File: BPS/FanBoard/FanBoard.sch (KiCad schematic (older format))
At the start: 12 parts, among them J1 Conn_01x02, J2 Conn_01x02, J3 Conn_01x02, J4 Conn_01x02, Q1 BUK9M34-100EX, Q2 BUK9M34-100EX, Q3 BUK9M34-100EX, Q4 BUK9M34-100EX

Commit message: Finished PCB
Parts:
- J1, J2, J3, J4: footprint (none) -> Connector_PinSocket_2.54mm:PinSocket_1x02_P2.54mm_Vertical
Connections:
- net at J1.2 (Pin_2), Q1.5 (D): now also D1.2 (A)
- net at J3.2 (Pin_2), Q3.5 (D): now also D3.2 (A)
- net at J4.2 (Pin_2), Q4.5 (D): now also D4.2 (A)
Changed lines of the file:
@@
 F 0 "J1" H 4330 3642 50  0000 L CNN
 F 1 "Conn_01x02" H 4330 3551 50  0000 L CNN
-F 2 "" H 4250 3650 50  0001 C CNN
+F 2 "Connector_PinSocket_2.54mm:PinSocket_1x02_P2.54mm_Vertical" H 4250 3650 50  0001 C CNN
 F 3 "~" H 4250 3650 50  0001 C CNN
 	1    4250 3650
@@
 F 0 "J2" H 4330 4292 50  0000 L CNN
 F 1 "Conn_01x02" H 4330 4201 50  0000 L CNN
-F 2 "" H 4250 4300 50  0001 C CNN
+F 2 "Connector_PinSocket_2.54mm:PinSocket_1x02_P2.54mm_Vertical" H 4250 4300 50  0001 C CNN
 F 3 "~" H 4250 4300 50  0001 C CNN
 	1    4250 4300
@@
 F 0 "J3" H 4330 4942 50  0000 L CNN
 F 1 "Conn_01x02" H 4330 4851 50  0000 L CNN
-F 2 "" H 4250 4950 50  0001 C CNN
+F 2 "Connector_PinSocket_2.54mm:PinSocket_1x02_P2.54mm_Vertical" H 4250 4950 50  0001 C CNN
 F 3 "~" H 4250 4950 50  0001 C CNN
 	1    4250 4950
@@
 F 0 "J4" H 4330 5592 50  0000 L CNN
 F 1 "Conn_01x02" H 4330 5501 50  0000 L CNN
-F 2 "" H 4250 5600 50  0001 C CNN
+F 2 "Connector_PinSocket_2.54mm:PinSocket_1x02_P2.54mm_Vertical" H 4250 5600 50  0001 C CNN
 F 3 "~" H 4250 5600 50  0001 C CNN
 	1    4250 5600
@@
 	3200 4400 3700 4400
 Wire Wire Line
-	3200 5050 4050 5050
-Wire Wire Line
-	3200 3750 4050 3750
+	3200 5050 3700 5050
+Wire Wire Line
+	3200 3750 3700 3750
 NoConn ~ 2900 5900
 NoConn ~ 2900 5250
@@
 $EndComp
 Wire Wire Line
-	3200 5700 4050 5700
+	3200 5700 3750 5700
 Connection ~ 3700 4400
 Wire Wire Line
@@
 Wire Wire Line
 	3950 5400 3950 4950
+Connection ~ 3700 3750
+Wire Wire Line
+	3700 3750 4050 3750
+Connection ~ 3700 5050
+Wire Wire Line
+	3700 5050 4050 5050
+Connection ~ 3750 5700
+Wire Wire Line
+	3750 5700 4050 5700
 $EndSCHEMATC

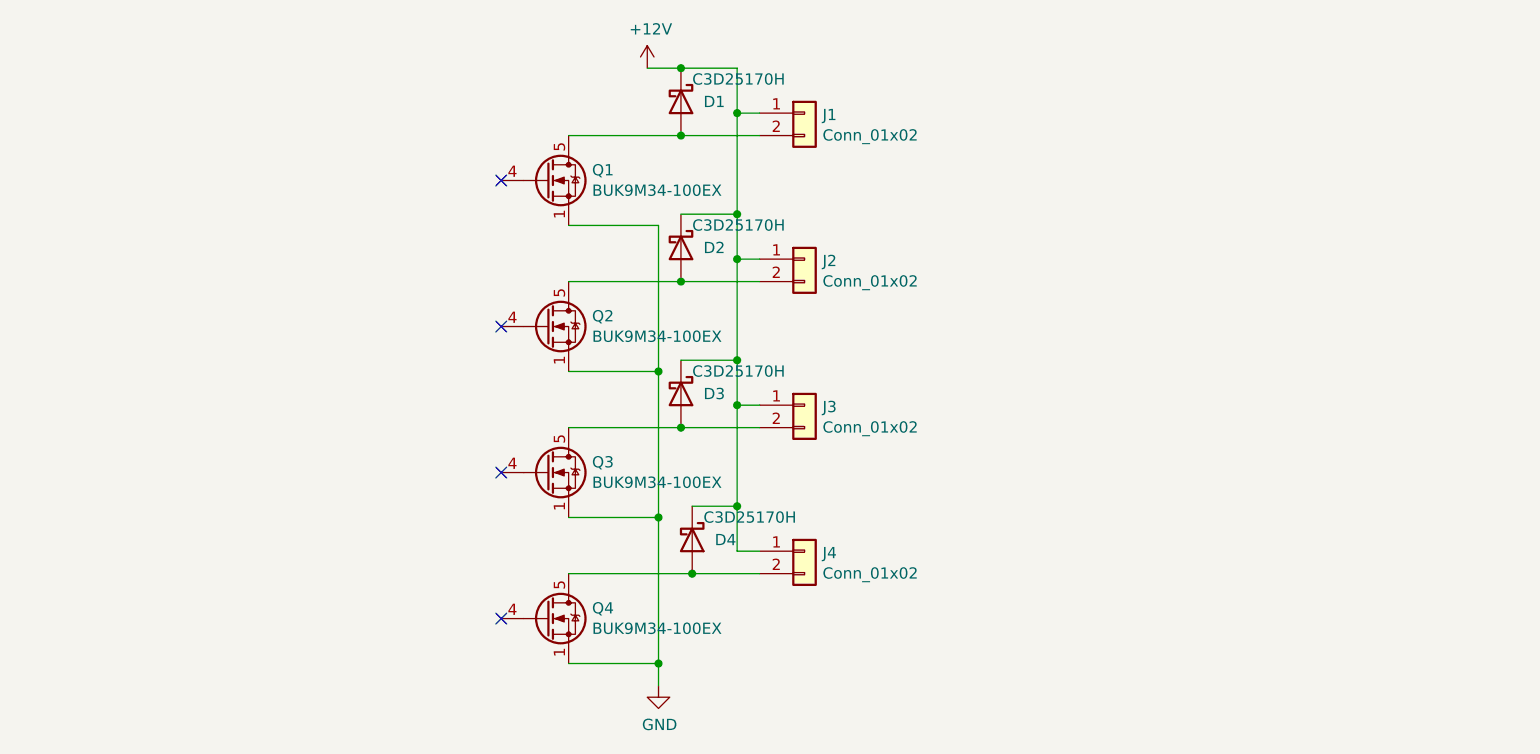
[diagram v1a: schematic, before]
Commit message: Added connections for control, pwr, and ground. Need to add DC-DC converter for 12V to 5V
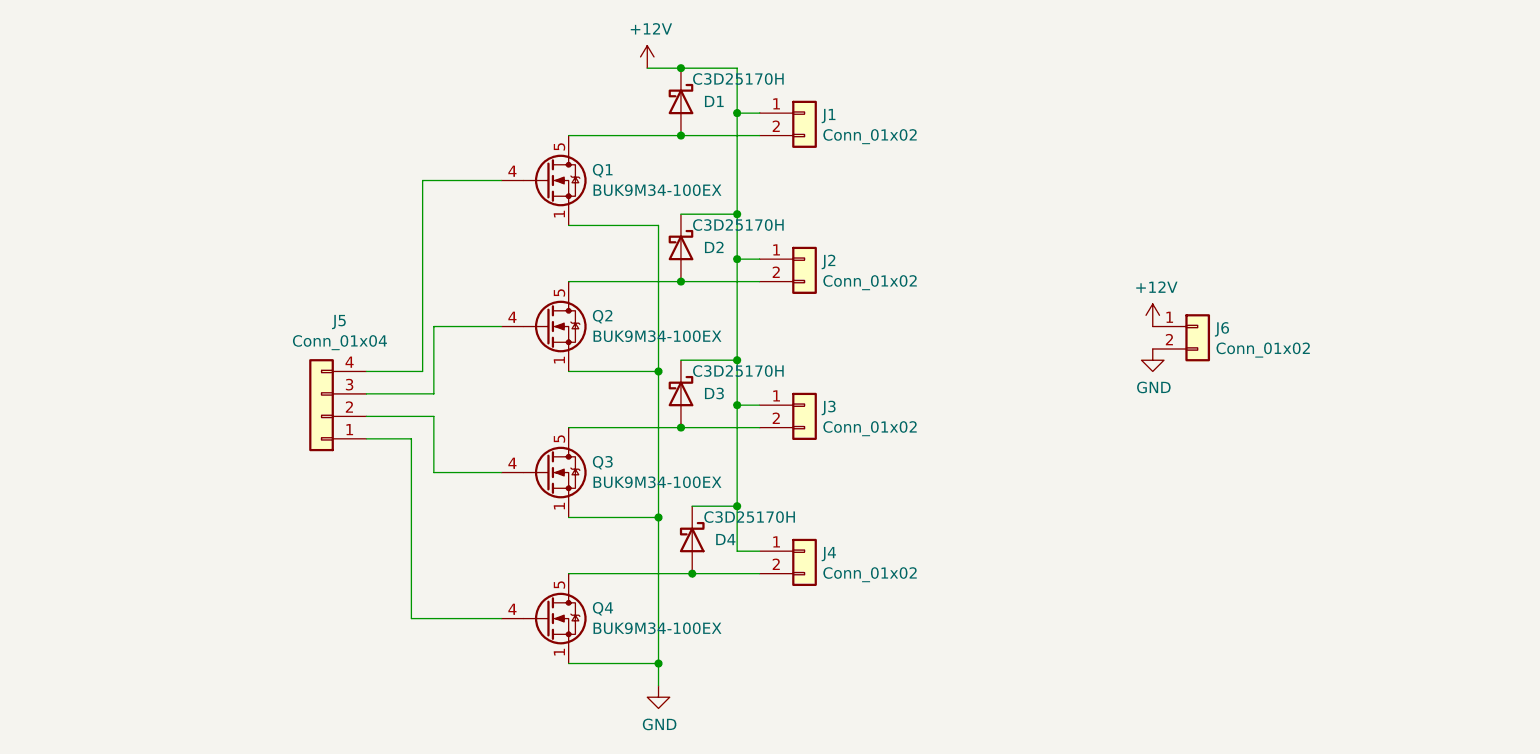
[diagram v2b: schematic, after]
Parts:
- added J5: Conn_01x04, symbol Connector_Generic:Conn_01x04
- added J6: Conn_01x02, symbol Connector_Generic:Conn_01x02
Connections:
- net +12V: now also J6.1 (Pin_1)
- net GND: now also J6.2 (Pin_2)
- net at Q1.4 (G): now also J5.4 (Pin_4)
- net at Q2.4 (G): now also J5.3 (Pin_3)
- net at Q3.4 (G): now also J5.2 (Pin_2)
- net at Q4.4 (G): now also J5.1 (Pin_1)
- no-connect marks 4 -> 0
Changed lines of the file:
@@
 Wire Wire Line
 	3200 3750 3700 3750
-NoConn ~ 2900 5900
-NoConn ~ 2900 5250
-NoConn ~ 2900 4600
-NoConn ~ 2900 3950
 $Comp
 L Transistor_FET:BUK9M34-100EX Q1
@@
 Wire Wire Line
 	3750 5700 4050 5700
+$Comp
+L Connector_Generic:Conn_01x04 J5
+U 1 1 5F0D21DB
+P 2100 5000
+F 0 "J5" H 2018 4575 50  0000 C CNN
+F 1 "Conn_01x04" H 2018 4666 50  0000 C CNN
+F 2 "" H 2100 5000 50  0001 C CNN
+F 3 "~" H 2100 5000 50  0001 C CNN
+	1    2100 5000
+	-1   0    0    1
+$EndComp
+Wire Wire Line
+	2900 3950 2550 3950
+Wire Wire Line
+	2550 3950 2550 4800
+Wire Wire Line
+	2550 4800 2300 4800
+Wire Wire Line
+	2900 4600 2600 4600
+Wire Wire Line
+	2600 4600 2600 4900
+Wire Wire Line
+	2600 4900 2300 4900
+Wire Wire Line
+	2900 5250 2600 5250
+Wire Wire Line
+	2600 5250 2600 5000
+Wire Wire Line
+	2600 5000 2300 5000
+Wire Wire Line
+	2900 5900 2500 5900
+Wire Wire Line
+	2500 5900 2500 5100
+Wire Wire Line
+	2500 5100 2300 5100
+$Comp
+L Connector_Generic:Conn_01x02 J6
+U 1 1 5F0D63BD
+P 6000 4600
+F 0 "J6" H 6080 4592 50  0000 L CNN
+F 1 "Conn_01x02" H 6080 4501 50  0000 L CNN
+F 2 "" H 6000 4600 50  0001 C CNN
+F 3 "~" H 6000 4600 50  0001 C CNN
+	1    6000 4600
+	1    0    0    -1
+$EndComp
+$Comp
+L power:+12V #PWR03
+U 1 1 5F0D67AB
+P 5800 4600
+F 0 "#PWR03" H 5800 4450 50  0001 C CNN
+F 1 "+12V" H 5815 4773 50  0000 C CNN
+F 2 "" H 5800 4600 50  0001 C CNN
+F 3 "" H 5800 4600 50  0001 C CNN
+	1    5800 4600
+	1    0    0    -1
+$EndComp
+$Comp
+L power:GND #PWR04
+U 1 1 5F0D6BE0
+P 5800 4700
+F 0 "#PWR04" H 5800 4450 50  0001 C CNN
+F 1 "GND" H 5805 4527 50  0000 C CNN
+F 2 "" H 5800 4700 50  0001 C CNN
+F 3 "" H 5800 4700 50  0001 C CNN
+	1    5800 4700
+	1    0    0    -1
+$EndComp
 $EndSCHEMATC

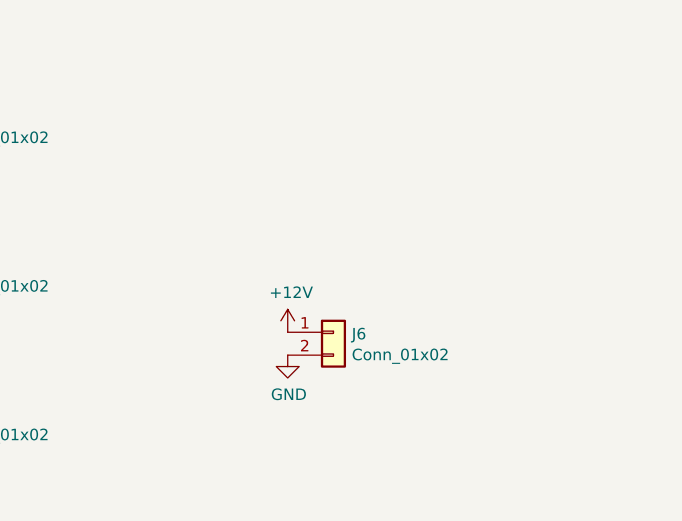
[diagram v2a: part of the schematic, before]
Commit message: Added DCDC converter for 12V-5V power supply
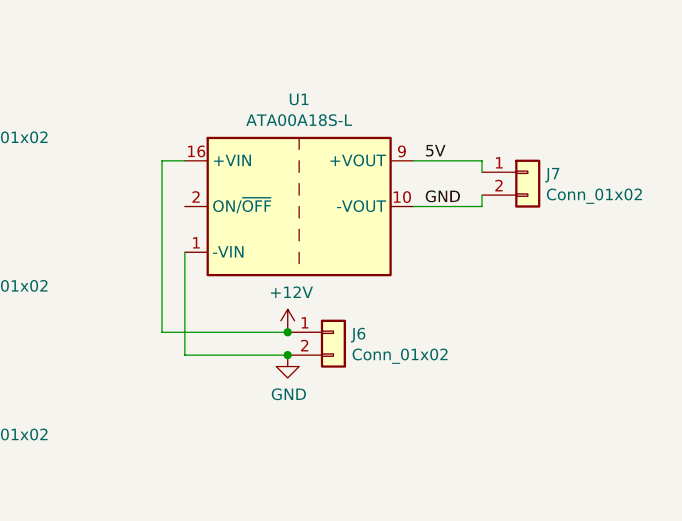
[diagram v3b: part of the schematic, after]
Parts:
- added J7: Conn_01x02, symbol Connector_Generic:Conn_01x02
- added U1: ATA00A18S-L, Converter_DCDC:Converter_DCDC_Artesyn_ATA_SMD, symbol Converter_DCDC:ATA00A18S-L
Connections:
- net +12V: now also U1.16 (+VIN)
- net GND: now also J7.2 (Pin_2), U1.1 (-VIN), U1.10 (-VOUT)
- new net 5V: J7.1 (Pin_1), U1.9 (+VOUT)
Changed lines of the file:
@@
 	1    0    0    -1
 $EndComp
+$Comp
+L Converter_DCDC:ATA00A18S-L U1
+U 1 1 5F104936
+P 5850 4050
+F 0 "U1" H 5850 4517 50  0000 C CNN
+F 1 "ATA00A18S-L" H 5850 4426 50  0000 C CNN
+F 2 "Converter_DCDC:Converter_DCDC_Artesyn_ATA_SMD" H 5850 3700 50  0001 C CIN
+F 3 "https://www.artesyn.com/power/assets/ata_series_ds_01apr2015_79c25814fd.pdf" H 5850 3600 50  0001 C CNN
+	1    5850 4050
+	1    0    0    -1
+$EndComp
+Wire Wire Line
+	5800 4600 5250 4600
+Wire Wire Line
+	5250 4600 5250 3850
+Wire Wire Line
+	5250 3850 5350 3850
+Connection ~ 5800 4600
+Wire Wire Line
+	5800 4700 5350 4700
+Wire Wire Line
+	5350 4700 5350 4250
+Connection ~ 5800 4700
+$Comp
+L Connector_Generic:Conn_01x02 J7
+U 1 1 5F1077A2
+P 6850 3900
+F 0 "J7" H 6930 3892 50  0000 L CNN
+F 1 "Conn_01x02" H 6930 3801 50  0000 L CNN
+F 2 "" H 6850 3900 50  0001 C CNN
+F 3 "~" H 6850 3900 50  0001 C CNN
+	1    6850 3900
+	1    0    0    -1
+$EndComp
+Wire Wire Line
+	6350 3850 6650 3850
+Wire Wire Line
+	6650 3850 6650 3900
+Wire Wire Line
+	6350 4050 6650 4050
+Wire Wire Line
+	6650 4050 6650 4000
+Text Label 6400 3850 0    50   ~ 0
+5V
+Text Label 6400 4050 0    50   ~ 0
+GND
 $EndSCHEMATC

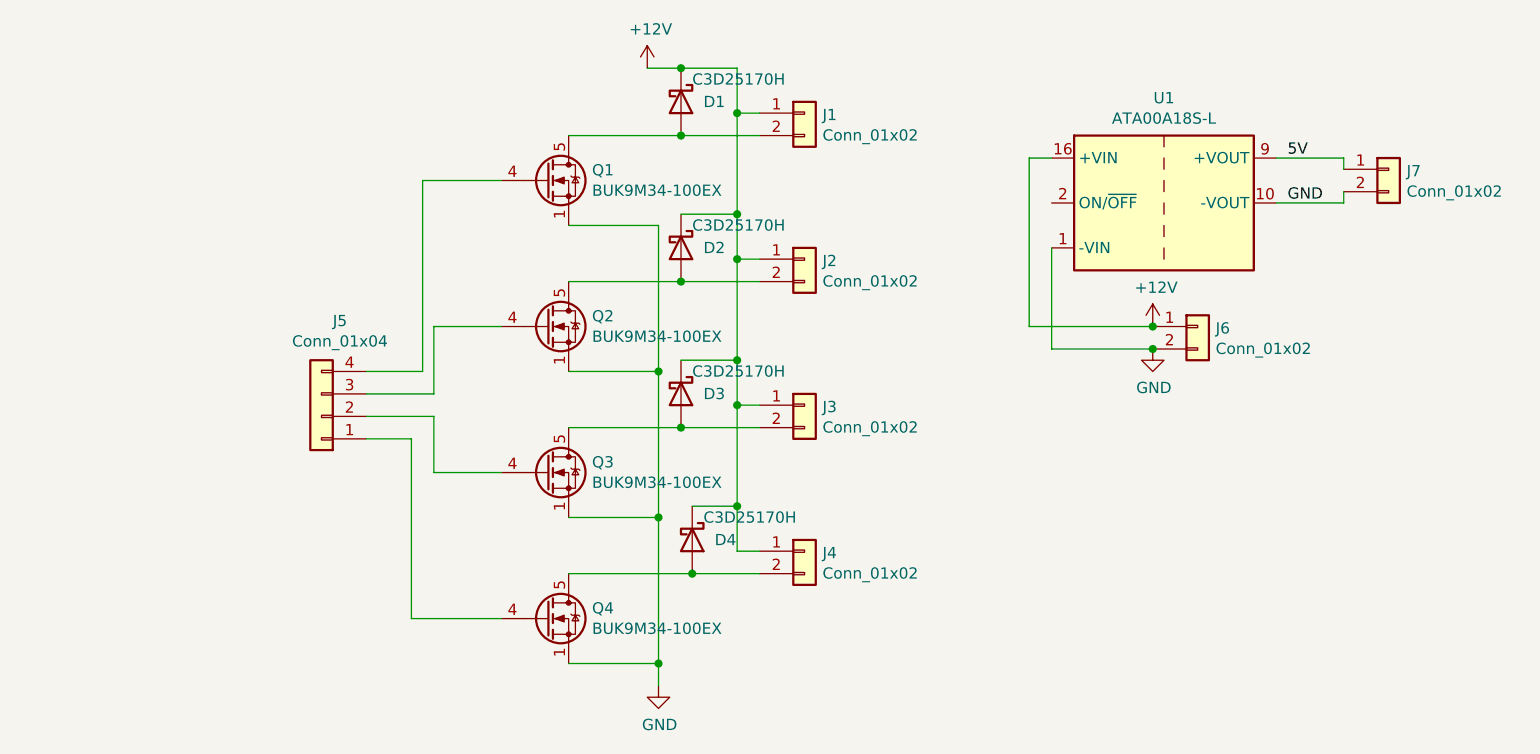
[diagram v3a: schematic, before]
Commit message: Removed dc converter and power connectors.
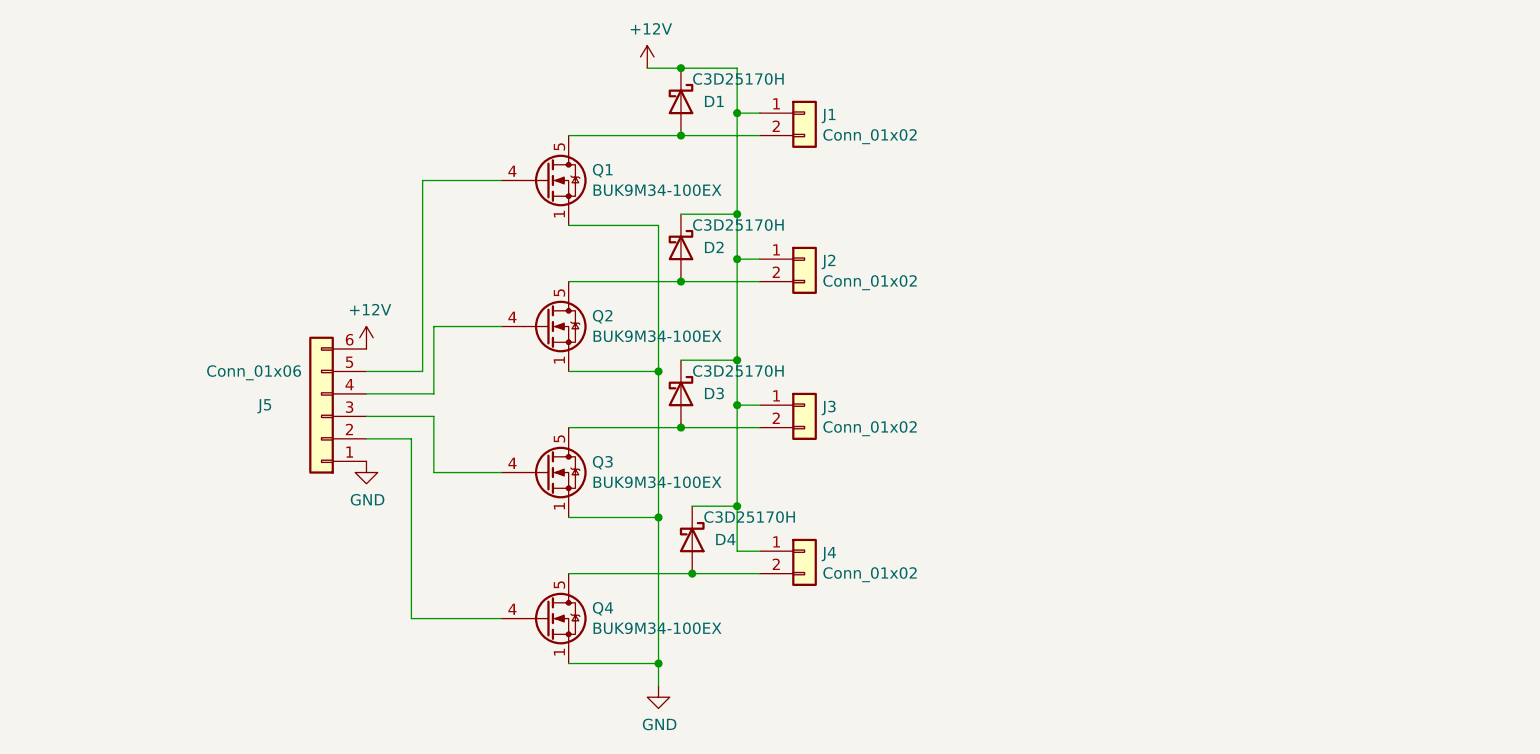
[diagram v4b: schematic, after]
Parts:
- removed J5: Conn_01x04, symbol Connector_Generic:Conn_01x04
- removed J6, J7: Conn_01x02, symbol Connector_Generic:Conn_01x02
- removed U1: ATA00A18S-L, Converter_DCDC:Converter_DCDC_Artesyn_ATA_SMD, symbol Converter_DCDC:ATA00A18S-L
- added J5: Conn_01x06, symbol Connector_Generic:Conn_01x06
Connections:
- net +12V: now also J5.6 (Pin_6)
- net GND: now also J5.1 (Pin_1)
- net at Q1.4 (G): now also J5.5 (Pin_5)
- net at Q2.4 (G): now also J5.4 (Pin_4)
- net at Q3.4 (G): now also J5.3 (Pin_3)
- net at Q4.4 (G): now also J5.2 (Pin_2)
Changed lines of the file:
@@
 Wire Wire Line
 	3750 5700 4050 5700
-$Comp
-L Connector_Generic:Conn_01x04 J5
-U 1 1 5F0D21DB
-P 2100 5000
-F 0 "J5" H 2018 4575 50  0000 C CNN
-F 1 "Conn_01x04" H 2018 4666 50  0000 C CNN
-F 2 "" H 2100 5000 50  0001 C CNN
-F 3 "~" H 2100 5000 50  0001 C CNN
-	1    2100 5000
-	-1   0    0    1
-$EndComp
 Wire Wire Line
 	2900 3950 2550 3950
@@
 	2500 5100 2300 5100
 $Comp
-L Connector_Generic:Conn_01x02 J6
-U 1 1 5F0D63BD
-P 6000 4600
-F 0 "J6" H 6080 4592 50  0000 L CNN
-F 1 "Conn_01x02" H 6080 4501 50  0000 L CNN
-F 2 "" H 6000 4600 50  0001 C CNN
-F 3 "~" H 6000 4600 50  0001 C CNN
-	1    6000 4600
-	1    0    0    -1
+L Connector_Generic:Conn_01x06 J5
+U 1 1 5F1BB034
+P 2100 5000
+F 0 "J5" H 2350 4950 50  0000 C CNN
+F 1 "Conn_01x06" H 2400 4800 50  0000 C CNN
+F 2 "" H 2100 5000 50  0001 C CNN
+F 3 "~" H 2100 5000 50  0001 C CNN
+	1    2100 5000
+	-1   0    0    1
 $EndComp
 $Comp
 L power:+12V #PWR03
-U 1 1 5F0D67AB
-P 5800 4600
-F 0 "#PWR03" H 5800 4450 50  0001 C CNN
-F 1 "+12V" H 5815 4773 50  0000 C CNN
-F 2 "" H 5800 4600 50  0001 C CNN
-F 3 "" H 5800 4600 50  0001 C CNN
-	1    5800 4600
+U 1 1 5F1BC556
+P 2300 4700
+F 0 "#PWR03" H 2300 4550 50  0001 C CNN
+F 1 "+12V" H 2315 4873 50  0000 C CNN
+F 2 "" H 2300 4700 50  0001 C CNN
+F 3 "" H 2300 4700 50  0001 C CNN
+	1    2300 4700
 	1    0    0    -1
 $EndComp
 $Comp
 L power:GND #PWR04
-U 1 1 5F0D6BE0
-P 5800 4700
-F 0 "#PWR04" H 5800 4450 50  0001 C CNN
-F 1 "GND" H 5805 4527 50  0000 C CNN
-F 2 "" H 5800 4700 50  0001 C CNN
-F 3 "" H 5800 4700 50  0001 C CNN
-	1    5800 4700
+U 1 1 5F1BCBA1
+P 2300 5200
+F 0 "#PWR04" H 2300 4950 50  0001 C CNN
+F 1 "GND" H 2305 5027 50  0000 C CNN
+F 2 "" H 2300 5200 50  0001 C CNN
+F 3 "" H 2300 5200 50  0001 C CNN
+	1    2300 5200
 	1    0    0    -1
 $EndComp
-$Comp
-L Converter_DCDC:ATA00A18S-L U1
-U 1 1 5F104936
-P 5850 4050
-F 0 "U1" H 5850 4517 50  0000 C CNN
-F 1 "ATA00A18S-L" H 5850 4426 50  0000 C CNN
-F 2 "Converter_DCDC:Converter_DCDC_Artesyn_ATA_SMD" H 5850 3700 50  0001 C CIN
-F 3 "https://www.artesyn.com/power/assets/ata_series_ds_01apr2015_79c25814fd.pdf" H 5850 3600 50  0001 C CNN
-	1    5850 4050
-	1    0    0    -1
-$EndComp
-Wire Wire Line
-	5800 4600 5250 4600
-Wire Wire Line
-	5250 4600 5250 3850
-Wire Wire Line
-	5250 3850 5350 3850
-Connection ~ 5800 4600
-Wire Wire Line
-	5800 4700 5350 4700
-Wire Wire Line
-	5350 4700 5350 4250
-Connection ~ 5800 4700
-$Comp
-L Connector_Generic:Conn_01x02 J7
-U 1 1 5F1077A2
-P 6850 3900
-F 0 "J7" H 6930 3892 50  0000 L CNN
-F 1 "Conn_01x02" H 6930 3801 50  0000 L CNN
-F 2 "" H 6850 3900 50  0001 C CNN
-F 3 "~" H 6850 3900 50  0001 C CNN
-	1    6850 3900
-	1    0    0    -1
-$EndComp
-Wire Wire Line
-	6350 3850 6650 3850
-Wire Wire Line
-	6650 3850 6650 3900
-Wire Wire Line
-	6350 4050 6650 4050
-Wire Wire Line
-	6650 4050 6650 4000
-Text Label 6400 3850 0    50   ~ 0
-5V
-Text Label 6400 4050 0    50   ~ 0
-GND
 $EndSCHEMATC
